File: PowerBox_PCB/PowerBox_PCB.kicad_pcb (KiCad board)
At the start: 2 copper layers, 100 x 75 mm, 112 parts, among them SW1 SW_DPDT_x2, U10 BQ25887RGER

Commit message: .
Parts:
- removed TP6, TP8: ~, Custom_Footprints:PAD-2x2
- added TP18: ~, Custom_Footprints:PAD-2x2-ThroughHole, F.Cu at (152.2, 84.2)
- added TP19: ~, Custom_Footprints:PAD-2x2-ThroughHole, F.Cu at (152.2, 87.2)
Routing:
- net GND: track 16.7 -> 19.2 mm

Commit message: fix bom
bom
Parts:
- U1, U5: value ~ -> TPS54620
- U11, U15: value ~ -> DW01A
- U12, U2, U4, U6, U8: value ~ -> MMBT3906LT1G
- U13, U14, U16, U17: value ~ -> AO3400A
- U18: value ~ -> LM1084RS-5.0
- U20: value ~ -> HUSB238_002DD
- U21, U3, U7: value ~ -> DMP6023LE-13
- U9: value ~ -> 2N7002
- USBC2: value ~ -> USBC_Port
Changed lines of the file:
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@@
 			)
 		)
-		(property "Value" "~"
+		(property "Value" "TPS54620"
 			(at 0 3.135 0)
 			(layer "F.Fab")
@@
 			)
 		)
-		(property "Value" "~"
+		(property "Value" "TPS54620"
 			(at 0 3.135 0)
 			(layer "F.Fab")
@@
 			)
 		)
-		(property "Value" "~"
+		(property "Value" "DMP6023LE-13"
 			(at 0 4.5 0)
 			(layer "F.Fab")
@@
 			)
 		)
-		(property "Value" "~"
+		(property "Value" "MMBT3906LT1G"
 			(at 0 2.4 0)
 			(layer "F.Fab")
@@
 			)
 		)
-		(property "Value" "~"
+		(property "Value" "HUSB238_002DD"
 			(at -0.014967 2.89 0)
 			(layer "F.Fab")
@@
 			)
 		)
-		(property "Value" "~"
+		(property "Value" "DW01A"
 			(at 0 2.9 0)
 			(layer "F.Fab")
@@
 			)
 		)
-		(property "Value" "~"
+		(property "Value" "MMBT3906LT1G"
 			(at 0 2.4 0)
 			(layer "F.Fab")
@@
 			)
 		)
-		(property "Value" "~"
+		(property "Value" "DW01A"
 			(at 0 2.9 0)
 			(layer "F.Fab")
@@
 			)
 		)
-		(property "Value" "~"
+		(property "Value" "AO3400A"
 			(at 0 2.5 90)
 			(layer "F.Fab")
@@
 			)
 		)
-		(property "Value" "~"
+		(property "Value" "DMP6023LE-13"
 			(at 0 4.5 90)
 			(layer "F.Fab")
@@
 			)
 		)
-		(property "Value" "~"
+		(property "Value" "LM1084RS-5.0"
 			(at 0 4.5 90)
 			(layer "F.Fab")
@@
 			)
 		)
-		(property "Value" "~"
+		(property "Value" "AO3400A"
 			(at 0 2.5 90)
 			(layer "F.Fab")
@@
 			)
 		)
-		(property "Value" "~"
+		(property "Value" "MMBT3906LT1G"
 			(at 0 2.4 0)
 			(layer "F.Fab")
@@
 			)
 		)
-		(property "Value" "~"
+		(property "Value" "AO3400A"
 			(at 0 2.5 90)
 			(layer "F.Fab")
@@
 			)
 		)
-		(property "Value" "~"
+		(property "Value" "MMBT3906LT1G"
 			(at 0 2.4 90)
 			(layer "F.Fab")
@@
 			)
 		)
-		(property "Value" "~"
+		(property "Value" "2N7002"
 			(at 0 2.4 0)
 			(layer "F.Fab")
@@
 			)
 		)
-		(property "Value" "~"
+		(property "Value" "AO3400A"
 			(at 0 2.5 90)
 			(layer "F.Fab")
@@
 			)
 		)
-		(property "Value" "~"
+		(property "Value" "MMBT3906LT1G"
 			(at 0 2.4 90)
 			(layer "F.Fab")
@@
 			)
 		)
-		(property "Value" "~"
+		(property "Value" "DMP6023LE-13"
 			(at 0 4.5 0)
 			(layer "F.Fab")
@@
 			)
 		)
-		(property "Value" "~"
+		(property "Value" "USBC_Port"
 			(at 0 6.0945 0)
 			(layer "F.Fab")

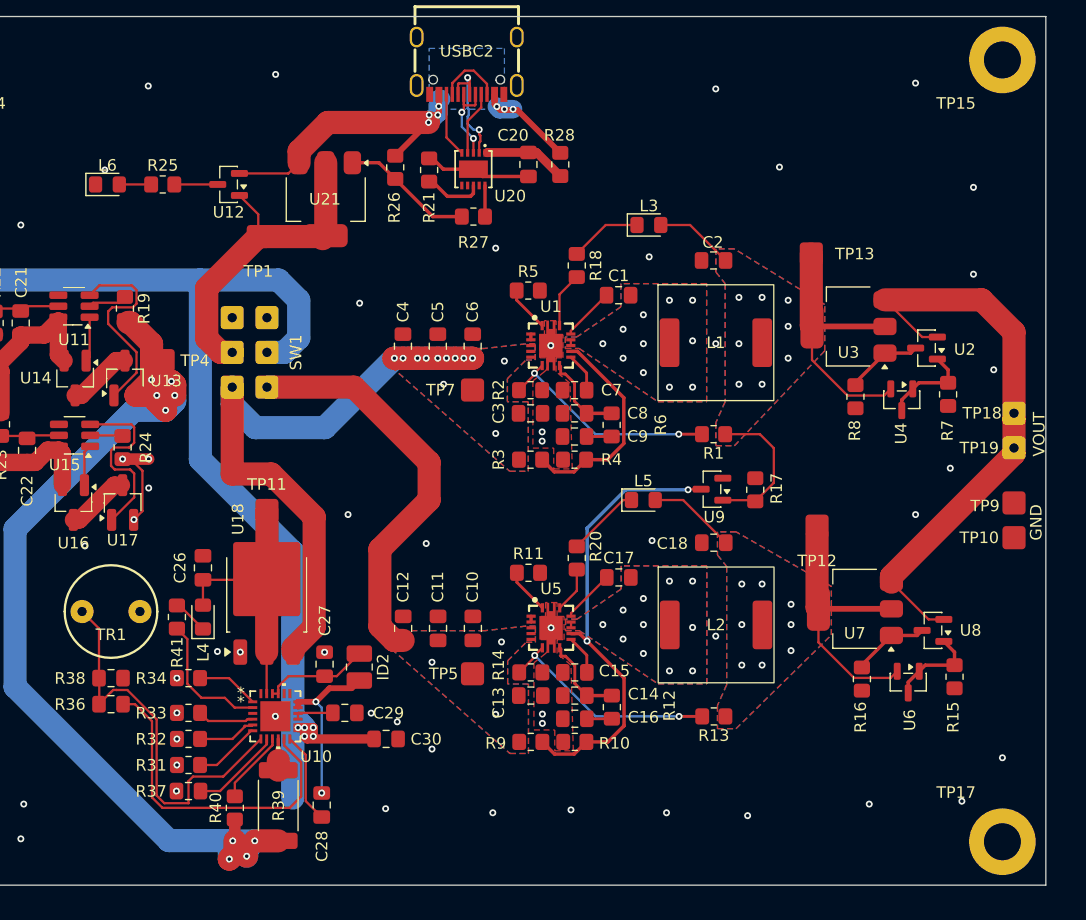
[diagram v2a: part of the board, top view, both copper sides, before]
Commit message: Changed HUSB238 to CH221K
HUSB238 Went out of stock so changed to CH221K
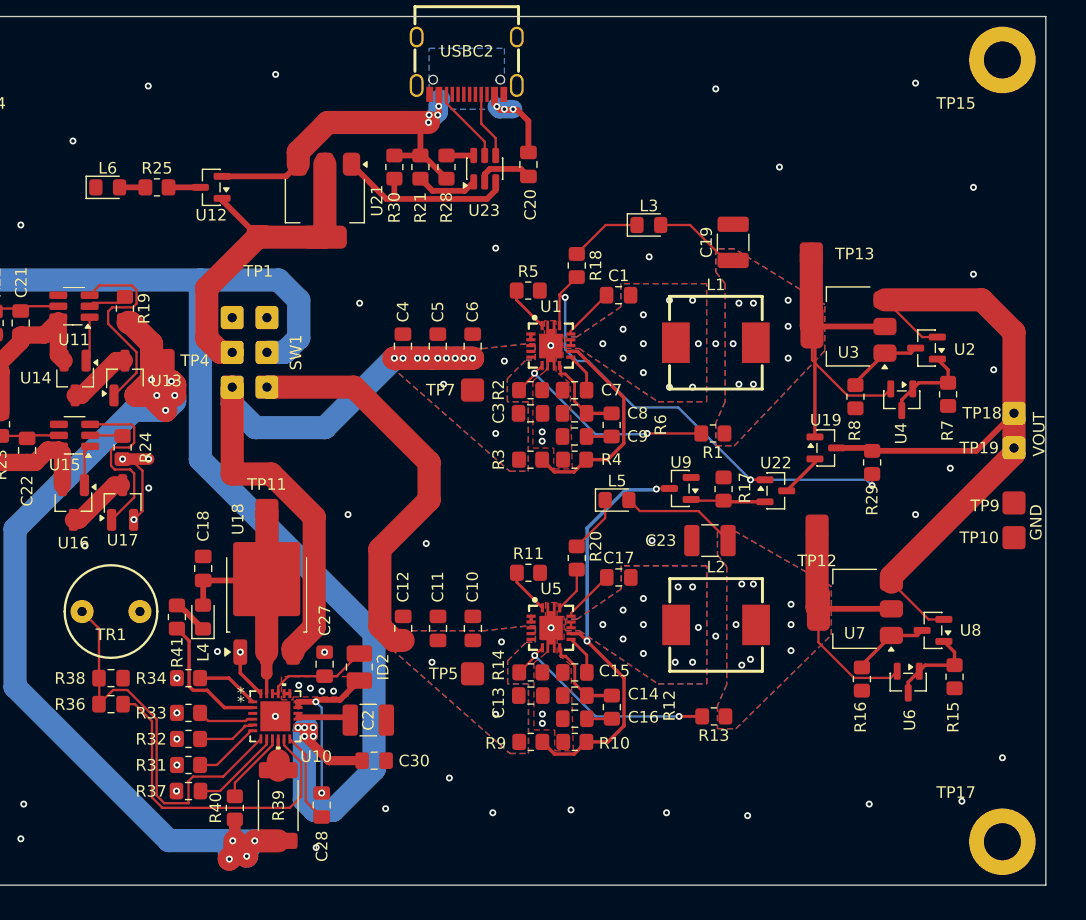
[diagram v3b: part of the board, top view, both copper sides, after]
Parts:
- removed C26: 1uF, Capacitor_SMD:C_0805_2012Metric_Pad1.18x1.45mm_HandSolder
- removed C29: 44uF, Capacitor_SMD:C_0805_2012Metric_Pad1.18x1.45mm_HandSolder
- removed R26: 49.9kΩ, Resistor_SMD:R_0805_2012Metric_Pad1.20x1.40mm_HandSolder
- removed R27: 5.1kΩ, Resistor_SMD:R_0805_2012Metric_Pad1.20x1.40mm_HandSolder
- removed U20: HUSB238_002DD, Custom_Footprints:DFN-10_L3.0-W3.0-P0.50-BL-EP2.5
- added C19: 47uF, Capacitor_SMD:C_1210_3225Metric_Pad1.33x2.70mm_HandSolder, F.Cu at (128.0, 69.5)
- added C23: 47uF, Capacitor_SMD:C_1210_3225Metric_Pad1.33x2.70mm_HandSolder, F.Cu at (126.0, 95.2)
- added R29: 10kΩ, Resistor_SMD:R_0805_2012Metric_Pad1.20x1.40mm_HandSolder, F.Cu at (140.0, 88.5)
- added R30: 100kΩ, Resistor_SMD:R_0805_2012Metric_Pad1.20x1.40mm_HandSolder, F.Cu at (98.8, 63.0)
- added U19: BC817, Package_TO_SOT_SMD:SOT-23, F.Cu at (136.0, 87.2)
- added U22: BC817, Package_TO_SOT_SMD:SOT-23, F.Cu at (131.7, 91.0)
- added U23: CH221K, Package_TO_SOT_SMD:SOT-23-6, F.Cu at (106.5, 63.1)
- C18: value 47uF -> 4.7uF
- C2: footprint Capacitor_SMD:C_0805_2012Metric_Pad1.18x1.45mm_HandSolder -> Capacitor_SMD:C_1210_3225Metric_Pad1.33x2.70mm_HandSolder
- L1, L2: footprint Buck_TPS54620:3.3uH_SMD,10x10mm -> Buck_TPS54620:IND-SMD_L8.5-W8.0_PSPMAA0803H-330M-ANP
- R21: value 10Ω -> 1kΩ
- R28: value 10Ω -> 100kΩ
- moved C2 49.6 mm to (96.5, 110.8), turned to 0 degrees
- moved C18 44.1 mm to (82.2, 97.7), turned to -90 degrees
- moved R28 9.83 mm to (103.2, 63.0), turned to 90 degrees
- moved R17 2.74 mm to (127.2, 90.8)
- moved U9 2.74 mm to (123.4, 90.8)
- moved L5 2.28 mm to (118.0, 91.8)
- moved C30 2.14 mm to (97.0, 114.2)
- moved U12 1.52 mm to (82.9, 64.8)
- moved R21 0.79 mm to (101.0, 63.0), turned to -90 degrees
- moved R25 0.56 mm to (78.2, 64.8)
- moved L6 0.25 mm to (74.0, 64.8)
- moved U21 0.15 mm to (92.8, 65.9)
- moved R1 0.09 mm to (126.2, 86.0)
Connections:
- C18 pad 1: /Ideal_Diode1/VIN_IDEAL -> GND
- C18 pad 2: GND -> /Batt Charger/VOUT
- C2 pad 1: /Ideal_Diode/VIN_IDEAL -> Net-(C2-Pad1)
- C20 pad 1: Net-(U20-VIN) -> /USBPD/VBUS
- R17 pad 1: /Ideal_Diode/VIN_IDEAL -> Net-(U22-E)
- R21 pad 1: Net-(U20-VSET) -> /USBPD/VBUS
- R21 pad 2: GND -> Net-(U23-VDD)
- R28 pad 2: Net-(U20-VIN) -> Net-(U23-CFG)
- U10 pad 15: Net-(C29-Pad1) -> Net-(C2-Pad1)
- U10 pad 16: Net-(C29-Pad1) -> Net-(C2-Pad1)
- U9 pad 1: /Ideal_Diode/VIN_IDEAL -> Net-(U22-E)
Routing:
- net /TPS54620_Buck/PWRGD_BUCK: track 4.80 -> 43.5 mm, vias 0 -> 3
- net /Ideal_Diode/VOUT_IDEAL: track 50.0 -> 66.7 mm
- net P+: track 112.4 -> 125.3 mm
- net /USBPD/D+: track 11.7 -> 0.00 mm, vias 2 -> 0
- net /USBPD/D-: track 8.38 -> 0.00 mm, vias 2 -> 0
- net Net-(U20-VIN): track 7.17 -> 0.00 mm
- net Net-(U22-E): track 0.00 -> 6.98 mm
- net /USBPD/SBUS: track 5.79 -> 0.00 mm
- net Net-(U23-VDD): track 0.00 -> 5.36 mm
- net Net-(C2-Pad1): track 0.00 -> 5.17 mm
- net Net-(U20-VSET): track 5.16 -> 0.00 mm
- net Net-(U21-G): track 11.4 -> 16.5 mm
- net /USBPD/VBUS: track 39.3 -> 44.2 mm
- net Net-(U19-E): track 0.00 -> 3.76 mm
- net Net-(C29-Pad1): track 3.53 -> 0.00 mm
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
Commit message: i finished and getting it made
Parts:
- removed R18, R20: 1kΩ, Resistor_SMD:R_0805_2012Metric_Pad1.20x1.40mm_HandSolder
- removed U18: LM1084RS-5.0, Package_TO_SOT_SMD:TO-252-3_TabPin2
- added R26: 2.2kΩ, Resistor_SMD:R_0805_2012Metric_Pad1.20x1.40mm_HandSolder, F.Cu at (114.5, 71.5)
- added R27: 2.2kΩ, Resistor_SMD:R_0805_2012Metric_Pad1.20x1.40mm_HandSolder, F.Cu at (114.5, 96.8)
- moved TP11 5.88 mm to (93.0, 90.0)
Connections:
- C18 pad 2: /Batt Charger/VOUT -> /VUSBOUT
- C19 pad 1: /Ideal_Diode/VIN_IDEAL -> /VUSBOUT
- L1 pad 2: /Ideal_Diode/VIN_IDEAL -> /VUSBOUT
- L3 pad 2: /Ideal_Diode/VIN_IDEAL -> /VUSBOUT
- L4 pad 2: /Batt Charger/VOUT -> /VUSBOUT
- R1 pad 1: /Ideal_Diode/VIN_IDEAL -> /VUSBOUT
- TP11 pad 1: /Batt Charger/VOUT -> /VUSBOUT
- TP13 pad 1: /Ideal_Diode/VIN_IDEAL -> /VUSBOUT
- U10 pad 23: /Batt Charger/VOUT -> /VUSBOUT
- U19 pad 1: /Ideal_Diode/VIN_IDEAL -> /VUSBOUT
- U3 pad 2: /Ideal_Diode/VIN_IDEAL -> /VUSBOUT
- U3 pad 4: /Ideal_Diode/VIN_IDEAL -> /VUSBOUT
- U4 pad 2: /Ideal_Diode/VIN_IDEAL -> /VUSBOUT
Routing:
- net /VUSBOUT: track 0.00 -> 150.3 mm, vias 0 -> 21
- net /Ideal_Diode/VIN_IDEAL: track 40.3 -> 0.00 mm, vias 8 -> 0
- net /VUSBPDSWITCHED: track 60.9 -> 32.4 mm
- net /Batt Charger/VOUT: track 25.8 -> 0.00 mm
- net /Batt Charger/SW: track 14.9 -> 16.5 mm
- added copper zone on B.Cu, net /VUSBOUT
- added copper zone on F.Cu, net /VUSBOUT
- removed copper zone on B.Cu, net /Ideal_Diode/VIN_IDEAL
- removed copper zone on F.Cu, net /Ideal_Diode/VIN_IDEAL
